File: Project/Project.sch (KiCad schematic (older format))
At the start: 33 parts, among them J1 Conn_01x05_Male, J2 USB_OTG, U1 CMWX1ZZABZ-078, U2 LM1117ADJ, Y1 8Mhz

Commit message: placed some more components
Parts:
- added D?: LED, symbol Device:LED
- added SW? (x2): SW_Push_Dual, symbol Switch:SW_Push_Dual
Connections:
- net 1pps(1_pulse_per_second): now also U1.24 (PA2/ADC2)
- net 3DF(3D-FiX_indicator): now also U1.23 (PA3/ADC3)
- net temperature: now reaches U1.22 (PA4/ADC4/DAC1)
- net temperature: now also U?.1 (Vout)
- no-connect marks 35 -> 31
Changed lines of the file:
@@
 NoConn ~ 9100 1500
 NoConn ~ 3350 2950
-NoConn ~ 3350 3050
-NoConn ~ 3350 3150
 NoConn ~ 3350 3250
 NoConn ~ 3350 3350
 NoConn ~ 3350 3450
-NoConn ~ 3350 3550
-NoConn ~ 3350 3650
 NoConn ~ 3350 3750
 NoConn ~ 3350 3850
@@
 Wire Wire Line
 	7600 3850 7750 3850
+Text Label 2950 3050 2    50   ~ 0
+1pps(1_pulse_per_second)
+Text Label 3150 3150 2    50   ~ 0
+3DF(3D-FiX_indicator)
+Wire Wire Line
+	2950 3050 3350 3050
+Wire Wire Line
+	3150 3150 3350 3150
+Text Label 8850 4250 0    50   ~ 0
+temperature
+Wire Wire Line
+	8850 4250 8250 4250
+Wire Wire Line
+	8250 4250 8250 4300
+Text Label 2850 3250 2    50   ~ 0
+temperature
+Wire Wire Line
+	2850 3250 3350 3250
+$Comp
+L Switch:SW_Push_Dual SW?
+U 1 1 5E40AB71
+P 7300 2850
+F 0 "SW?" H 7300 3135 50  0000 C CNN
+F 1 "SW_Push_Dual" H 7300 3044 50  0000 C CNN
+F 2 "" H 7300 3050 50  0001 C CNN
+F 3 "~" H 7300 3050 50  0001 C CNN
+	1    7300 2850
+	1    0    0    -1
+$EndComp
+$Comp
+L Switch:SW_Push_Dual SW?
+U 1 1 5E40D579
+P 6750 2850
+F 0 "SW?" H 6750 3135 50  0000 C CNN
+F 1 "SW_Push_Dual" H 6750 3044 50  0000 C CNN
+F 2 "" H 6750 3050 50  0001 C CNN
+F 3 "~" H 6750 3050 50  0001 C CNN
+	1    6750 2850
+	1    0    0    -1
+$EndComp
+$Comp
+L Device:LED D?
+U 1 1 5E40DD7F
+P 6700 2350
+F 0 "D?" H 6693 2566 50  0000 C CNN
+F 1 "LED" H 6693 2475 50  0000 C CNN
+F 2 "" H 6700 2350 50  0001 C CNN
+F 3 "~" H 6700 2350 50  0001 C CNN
+	1    6700 2350
+	1    0    0    -1
+$EndComp
 $EndSCHEMATC

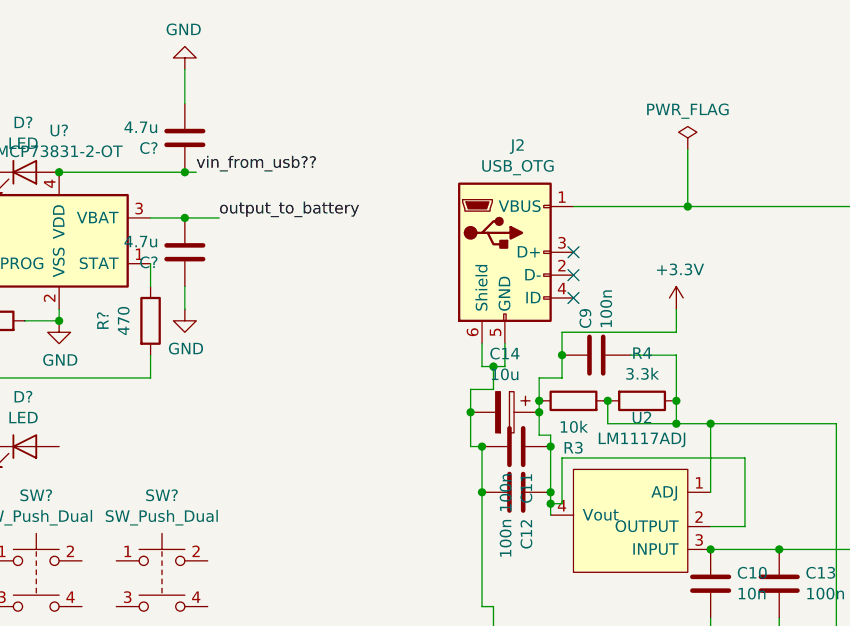
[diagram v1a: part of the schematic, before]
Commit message: Conn added for battery and some connections
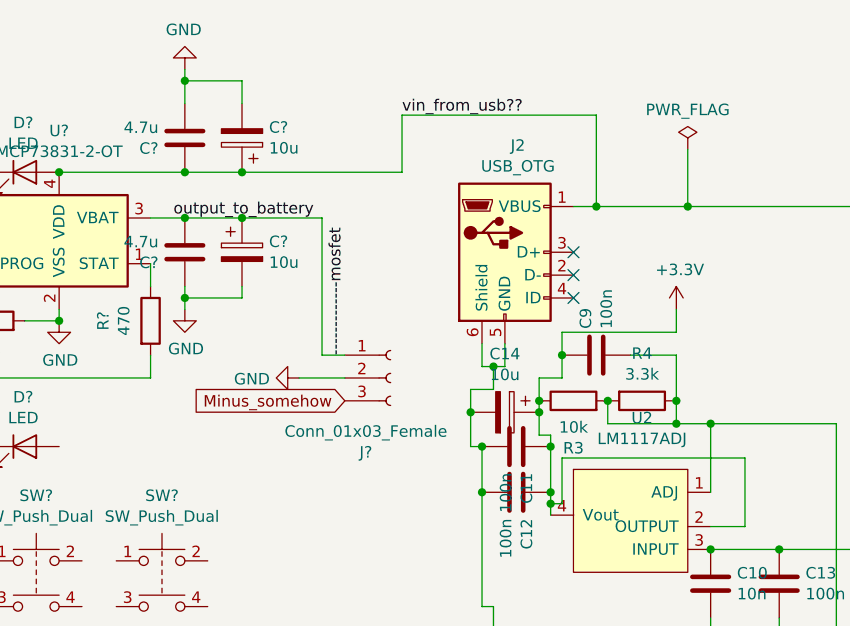
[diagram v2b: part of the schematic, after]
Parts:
- added C? (x2): 10u, symbol Device:CP
- added J?: Conn_01x03_Female, symbol Connector:Conn_01x03_Female
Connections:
- net GND: now also C?.2, C?.2, J?.2 (Pin_2)
- net vin_from_usb??: now also C10.1, C13.1, C15.1, J2.1 (VBUS), U2.3 (INPUT), C?.1
- net output_to_battery renamed -------------mosfet
- net -------------mosfet: now also C?.1, J?.1 (Pin_1)
- new net Minus_somehow: J?.3 (Pin_3)
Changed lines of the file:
@@
 	10650 2800 10500 2800
 Wire Wire Line
-	9100 1300 9600 1300
+	9100 1300 9200 1300
 Connection ~ 9700 2800
 NoConn ~ 5150 3050
@@
 	4600 2350 4450 2350
 $Comp
-L power:+3.3V #PWR?
+L power:+3.3V #PWR0109
 U 1 1 5E350560
 P 9550 1750
-F 0 "#PWR?" H 9550 1600 50  0001 C CNN
+F 0 "#PWR0109" H 9550 1600 50  0001 C CNN
 F 1 "+3.3V" H 9565 1923 50  0000 C CNN
 F 2 "" H 9550 1750 50  0001 C CNN
@@
 	3350 3550 1650 3550
 $Comp
-L power:+3.3V #PWR?
+L power:+3.3V #PWR0110
 U 1 1 5E3B7739
 P 2050 3250
-F 0 "#PWR?" H 2050 3100 50  0001 C CNN
+F 0 "#PWR0110" H 2050 3100 50  0001 C CNN
 F 1 "+3.3V" H 2065 3423 50  0000 C CNN
 F 2 "" H 2050 3250 50  0001 C CNN
@@
 	2050 3250 1650 3250
 $Comp
-L power:GND #PWR?
+L power:GND #PWR0111
 U 1 1 5E3C0420
 P 2150 3350
-F 0 "#PWR?" H 2150 3100 50  0001 C CNN
+F 0 "#PWR0111" H 2150 3100 50  0001 C CNN
 F 1 "GND" H 2155 3177 50  0000 C CNN
 F 2 "" H 2150 3350 50  0001 C CNN
@@
 	7250 2050 7250 1950
 $Comp
-L power:GND #PWR?
+L power:GND #PWR0112
 U 1 1 5E4178ED
 P 6850 1800
-F 0 "#PWR?" H 6850 1550 50  0001 C CNN
+F 0 "#PWR0112" H 6850 1550 50  0001 C CNN
 F 1 "GND" H 6855 1627 50  0000 C CNN
 F 2 "" H 6850 1800 50  0001 C CNN
@@
 $EndComp
 Connection ~ 6850 1800
-Text Label 7550 1350 0    50   ~ 0
+Text Label 7350 1350 0    50   ~ 0
 output_to_battery
 Connection ~ 6850 1150
-Text Label 7450 1150 0    50   ~ 0
+Text Label 8350 900  0    50   ~ 0
 vin_from_usb??
 $Comp
@@
 $EndComp
 $Comp
-L power:GND #PWR?
+L power:GND #PWR0113
 U 1 1 5E3FCED5
 P 7400 700
-F 0 "#PWR?" H 7400 450 50  0001 C CNN
+F 0 "#PWR0113" H 7400 450 50  0001 C CNN
 F 1 "GND" H 7405 527 50  0000 C CNN
 F 2 "" H 7400 700 50  0001 C CNN
@@
 $EndComp
 Wire Wire Line
-	7400 700  7400 850
-Wire Wire Line
-	7450 1150 7400 1150
+	7400 700  7400 750
 Wire Wire Line
 	6850 1150 7400 1150
@@
 	1    0    0    -1
 $EndComp
-Wire Wire Line
-	7550 1350 7400 1350
 $Comp
 L Device:C C?
@@
 	7400 1350 7250 1350
 $Comp
-L power:GND #PWR?
+L power:GND #PWR0114
 U 1 1 5E43DF37
 P 7400 1750
-F 0 "#PWR?" H 7400 1500 50  0001 C CNN
+F 0 "#PWR0114" H 7400 1500 50  0001 C CNN
 F 1 "GND" H 7405 1577 50  0000 C CNN
 F 2 "" H 7400 1750 50  0001 C CNN
@@
 $EndComp
 Wire Wire Line
-	7400 1750 7400 1650
+	7400 1750 7400 1700
 $Comp
 L Sensor_Temperature:TMP36xS U?
@@
 $EndComp
 $Comp
-L power:GND #PWR?
+L power:GND #PWR0115
 U 1 1 5E4A3FDE
 P 7750 4850
-F 0 "#PWR?" H 7750 4600 50  0001 C CNN
+F 0 "#PWR0115" H 7750 4600 50  0001 C CNN
 F 1 "GND" H 7755 4677 50  0000 C CNN
 F 2 "" H 7750 4850 50  0001 C CNN
@@
 $EndComp
 $Comp
-L power:GND #PWR?
+L power:GND #PWR0116
 U 1 1 5E4AD842
 P 7400 3550
-F 0 "#PWR?" H 7400 3300 50  0001 C CNN
+F 0 "#PWR0116" H 7400 3300 50  0001 C CNN
 F 1 "GND" H 7405 3377 50  0000 C CNN
 F 2 "" H 7400 3550 50  0001 C CNN
@@
 	1    0    0    -1
 $EndComp
+$Comp
+L Device:CP C?
+U 1 1 5E3EC996
+P 7650 1000
+F 0 "C?" H 7532 954 50  0000 R CNN
+F 1 "10u" H 7532 1045 50  0000 R CNN
+F 2 "" H 7688 850 50  0001 C CNN
+F 3 "~" H 7650 1000 50  0001 C CNN
+	1    7650 1000
+	-1   0    0    1
+$EndComp
+Wire Wire Line
+	7400 1150 7650 1150
+Wire Wire Line
+	7650 850  7650 750
+Wire Wire Line
+	7650 750  7400 750
+Connection ~ 7400 750
+Wire Wire Line
+	7400 750  7400 850
+Wire Wire Line
+	7650 1150 8350 1150
+Wire Wire Line
+	8350 1150 8350 900
+Wire Wire Line
+	8350 900  9200 900
+Wire Wire Line
+	9200 900  9200 1300
+Connection ~ 7650 1150
+Connection ~ 9200 1300
+Wire Wire Line
+	9200 1300 9600 1300
+$Comp
+L Connector:Conn_01x03_Female J?
+U 1 1 5E41D872
+P 8300 2050
+F 0 "J?" H 8192 1725 50  0000 C CNN
+F 1 "Conn_01x03_Female" H 8192 1816 50  0000 C CNN
+F 2 "" H 8300 2050 50  0001 C CNN
+F 3 "~" H 8300 2050 50  0001 C CNN
+	1    8300 2050
+	1    0    0    -1
+$EndComp
+Wire Wire Line
+	7400 1350 7650 1350
+$Comp
+L power:GND #PWR0117
+U 1 1 5E43C4C2
+P 7900 2050
+F 0 "#PWR0117" H 7900 1800 50  0001 C CNN
+F 1 "GND" V 7905 1922 50  0000 R CNN
+F 2 "" H 7900 2050 50  0001 C CNN
+F 3 "" H 7900 2050 50  0001 C CNN
+	1    7900 2050
+	0    1    1    0
+$EndComp
+Wire Wire Line
+	7900 2050 8100 2050
+Text GLabel 8100 2150 0    50   Input ~ 0
+Minus_somehow
+$Comp
+L Device:CP C?
+U 1 1 5E4732F3
+P 7650 1500
+F 0 "C?" H 7768 1546 50  0000 L CNN
+F 1 "10u" H 7768 1455 50  0000 L CNN
+F 2 "" H 7688 1350 50  0001 C CNN
+F 3 "~" H 7650 1500 50  0001 C CNN
+	1    7650 1500
+	1    0    0    -1
+$EndComp
+Connection ~ 7650 1350
+Wire Wire Line
+	7650 1350 8000 1350
+Wire Wire Line
+	7650 1650 7650 1700
+Wire Wire Line
+	7650 1700 7400 1700
+Connection ~ 7400 1700
+Wire Wire Line
+	7400 1700 7400 1650
+Wire Wire Line
+	8000 1350 8000 1950
+Wire Wire Line
+	8000 1950 8100 1950
+Text Label 8100 1950 1    50   ~ 0
+-------------mosfet
 $EndSCHEMATC

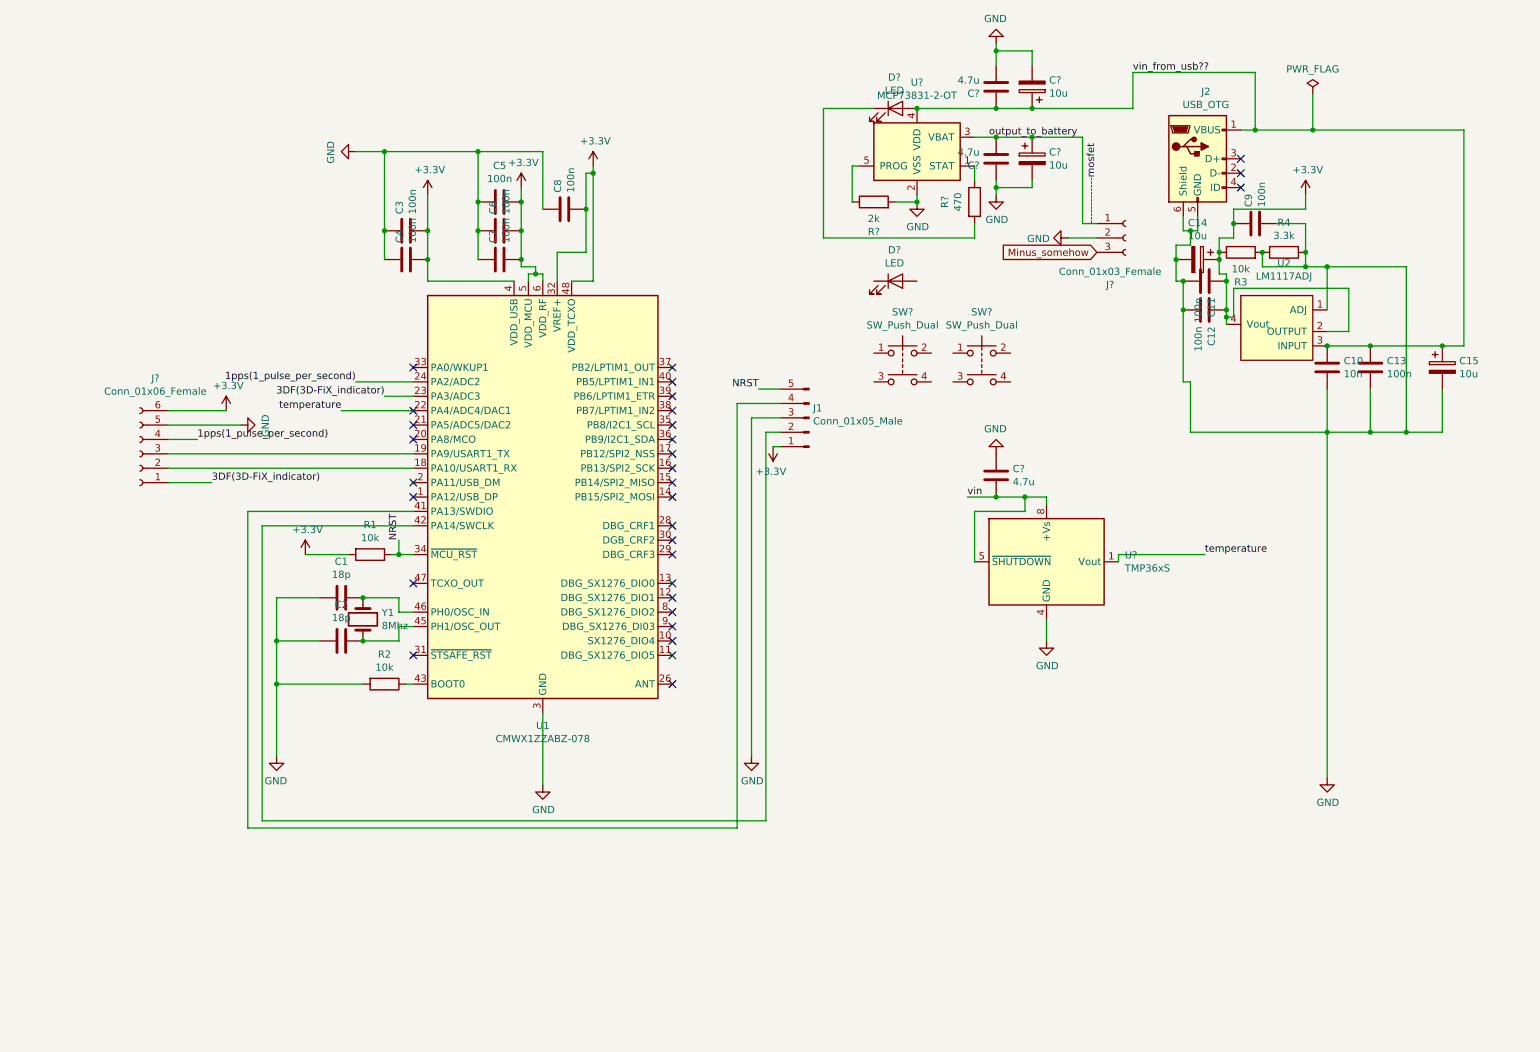
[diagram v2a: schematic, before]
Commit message: some more components and footprints
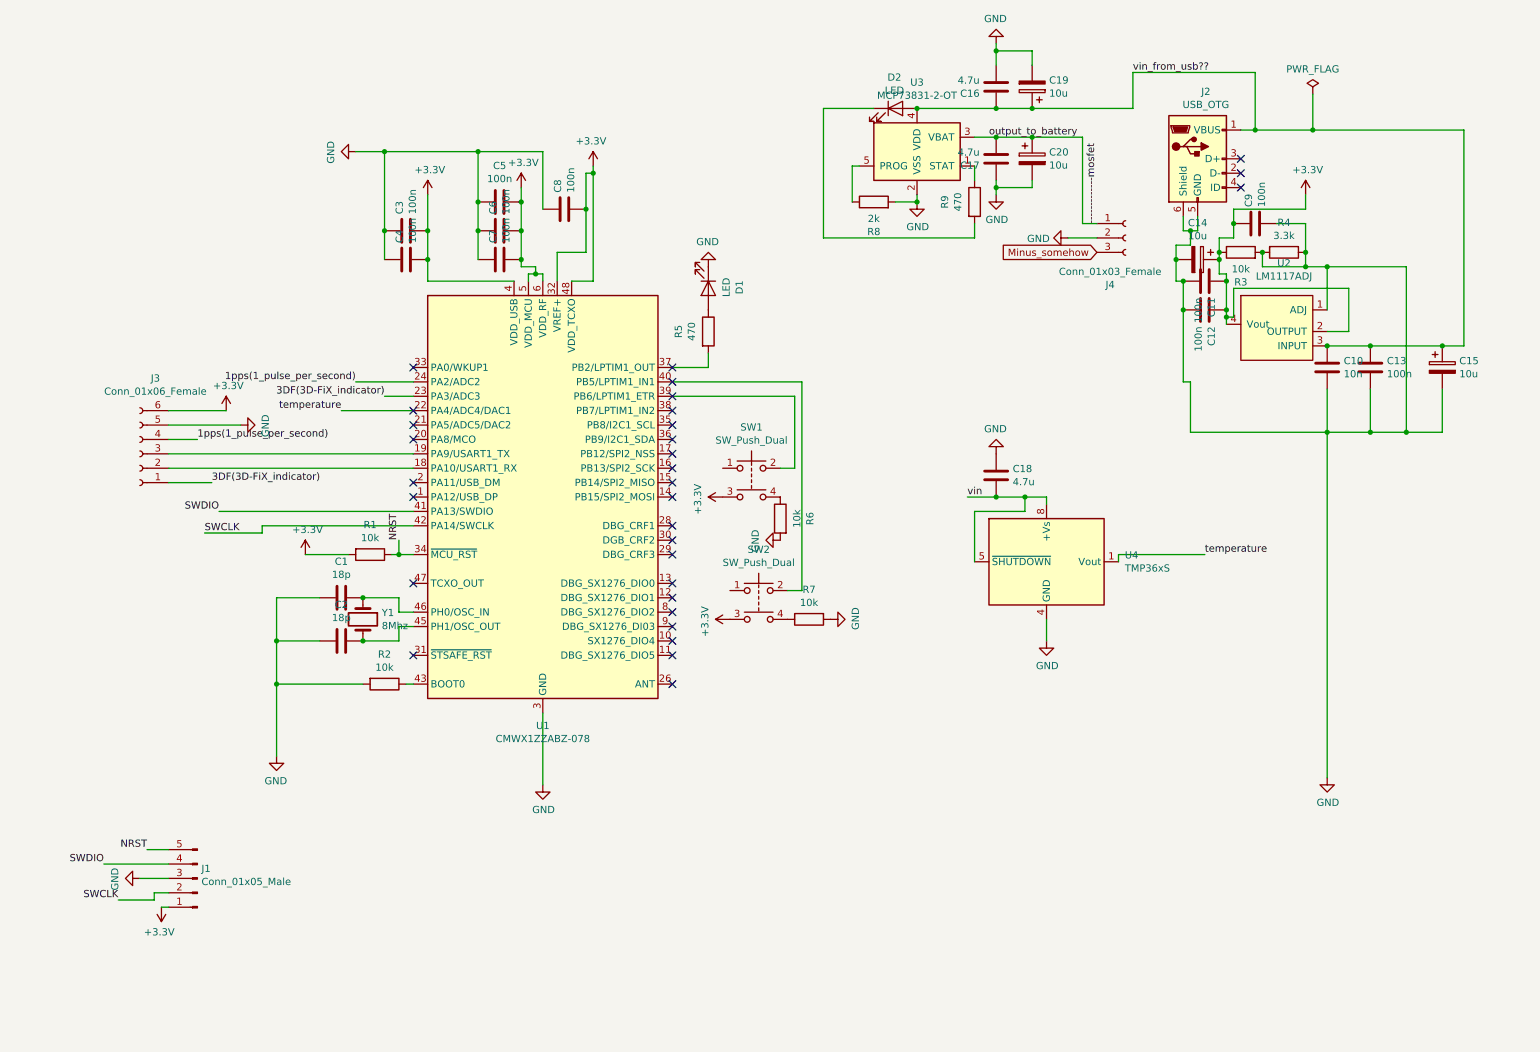
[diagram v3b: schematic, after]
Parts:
- added R5: 470, Resistor_SMD:R_0805_2012Metric_Pad1.15x1.40mm_HandSolder, symbol Device:R
- added R6, R7: 10k, Resistor_SMD:R_0805_2012Metric_Pad1.15x1.40mm_HandSolder, symbol Device:R
- SW1, SW2: renamed from SW?; footprint (none) -> Button_Switch_SMD:SW_Push_1P1T_NO_6x6mm_H9.5mm
- gave numbers to parts that had none: 13
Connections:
- net +3V3: now also SW1.3, SW2.3
- net GND: now also D1.1 (K), R6.2, R7.2
- net at U1.37 (PB2/LPTIM1_OUT): now also R5.2
- net at U1.39 (PB6/LPTIM1_ETR): now also SW1.2
- net at U1.40 (PB5/LPTIM1_IN1): now also SW2.2
- net SWDIO: now reaches J1.4 (Pin_4), U1.41 (PA13/SWDIO)
- net SWCLK: now reaches J1.2 (Pin_2), U1.42 (PA14/SWCLK)
- net at SW2.4: now also R7.1
- net at SW1.4: now also R6.1
- net at D1.2 (A): now also R5.1
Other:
- moved on the sheet: D1, J1, SW1, SW2

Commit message: more components and footprints
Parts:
- removed C2: 18p, Capacitor_SMD:C_0805_2012Metric_Pad1.15x1.40mm_HandSolder, symbol Device:C
- removed J3: Conn_01x06_Female, symbol Connector:Conn_01x06_Female
- removed R1: 10k, Resistor_SMD:R_0805_2012Metric_Pad1.15x1.40mm_HandSolder, symbol Device:R
- removed SW1, SW2: SW_Push_Dual, Button_Switch_SMD:SW_Push_1P1T_NO_6x6mm_H9.5mm, symbol Switch:SW_Push_Dual
- removed Y1: 8Mhz, Crystal:Crystal_HC49-U_Vertical, symbol Device:Crystal
- added C? (x2): 10u, Capacitor_SMD:C_0805_2012Metric_Pad1.15x1.40mm_HandSolder, symbol Device:C
- added C?: 100n, Capacitor_SMD:C_0805_2012Metric_Pad1.15x1.40mm_HandSolder, symbol Device:C
- added J3: Conn_01x09_Male, Connector_PinHeader_2.54mm:PinHeader_1x09_P2.54mm_Horizontal, symbol Connector:Conn_01x09_Male
- added J?: Conn_Coaxial, symbol Connector:Conn_Coaxial
- added SW1, SW2, SW3: SW_Push, Button_Switch_SMD:SW_Push_1P1T_NO_6x6mm_H9.5mm, symbol Switch:SW_Push
- C1: value 18p -> 0.1u
- C19, C20: footprint (none) -> Capacitor_SMD:C_0805_2012Metric_Pad1.15x1.40mm_HandSolder
- D1, D2: footprint (none) -> LED_SMD:LED_0805_2012Metric_Pad1.15x1.40mm_HandSolder
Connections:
- net +3V3: now also J3.1 (Pin_1), J3.8 (Pin_8), SW1.1, SW3.1
- net 1pps(1_pulse_per_second): now also J3.9 (Pin_9); no longer U1.24 (PA2/ADC2)
- net 3DF(3D-FiX_indicator): now also J3.4 (Pin_4)
- net GND: now also C?.1, C?.1, J3.7 (Pin_7), J?.2 (Ext), SW2.2
- net NRST: now also C1.1, SW2.1
- net TX: now reaches U1.18 (PA10/USART1_RX)
- net TX: now also J3.5 (Pin_5)
- net RX: now reaches U1.19 (PA9/USART1_TX)
- net RX: now also J3.6 (Pin_6)
- net at U1.26 (ANT): now also C?.1, C?.2
- net at U1.39 (PB6/LPTIM1_ETR): now also R6.1, SW1.2
- net at U1.40 (PB5/LPTIM1_IN1): now also R7.1, SW3.2
- net at U1.46 (PH0/OSC_IN): no longer C1.1
- new net: C?.2, C?.2, J?.1 (In)
- new net VbAt: J3.3 (Pin_3)
- new net enable: J3.2 (Pin_2)
- no-connect marks 31 -> 27
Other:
- moved on the sheet: J1
